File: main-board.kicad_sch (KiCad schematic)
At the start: 3 parts, among them J1 Battery, J25 Mikona

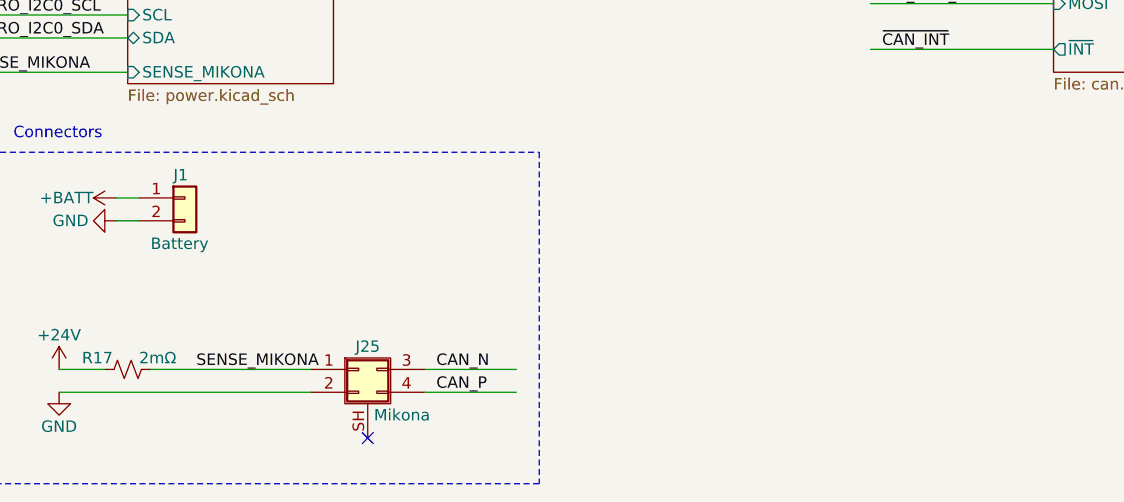
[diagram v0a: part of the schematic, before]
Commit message: Import the previous main board to match the overall shape, and re-annotate the schematic.
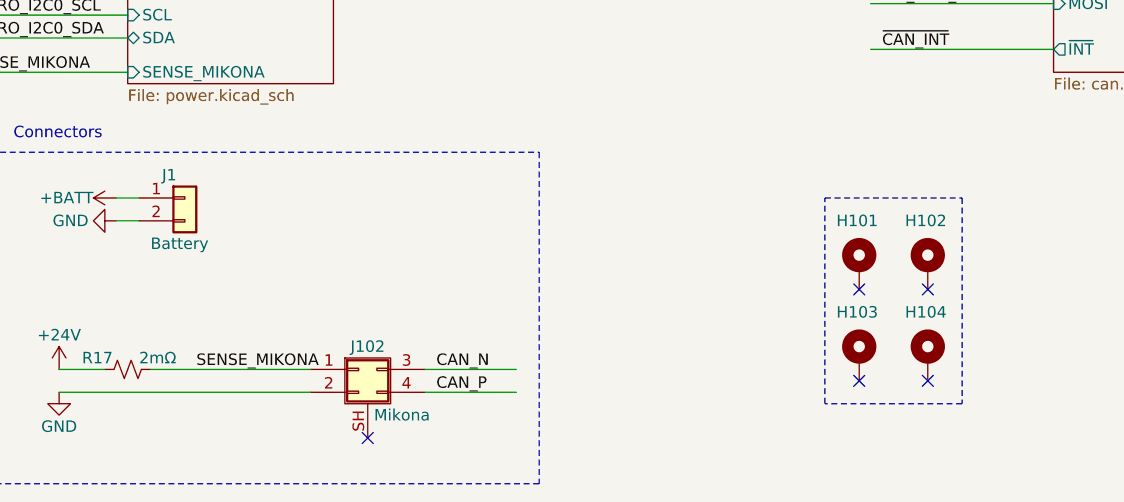
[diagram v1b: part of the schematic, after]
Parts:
- added H101, H102, H103, H104: MountingHole_Pad, MountingHole:MountingHole_3.2mm_M3_ISO14580_Pad, symbol Mechanical:MountingHole_Pad
- R17: footprint (none) -> Resistor_SMD:R_2512_6332Metric
- renumbered J25 to J102
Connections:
- no-connect marks 4 -> 8
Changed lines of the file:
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@@
 (kicad_sch (version 20230121) (generator eeschema)
   (paper "A4")
+  (no_connect (at 119.38 168.91))
   (no_connect (at 64.77 185.42))
+  (no_connect (at 119.38 179.07))
+  (no_connect (at 127 179.07))
   (no_connect (at 38.1 133.35))
   (no_connect (at 29.21 41.91))
   (no_connect (at 29.21 52.07))
+  (no_connect (at 127 168.91))
   (wire (pts (xy 120.65 134.62) (xy 140.97 134.62))
     (stroke (width 0) (type default))
@@
     (fill (type none))
   )
+  (rectangle (start 115.57 158.75) (end 130.81 181.61)
+    (stroke (width 0) (type dash))
+    (fill (type none))
+  )
   (text "Connectors" (at 25.4 152.4 0)
     (effects (font (size 1.27 1.27)) (justify left bottom))
@@
   (label "CM_SPI1_SCK" (at 121.92 132.08 0) (fields_autoplaced)
     (effects (font (size 1.27 1.27)) (justify left bottom))
+  )
+  (symbol (lib_id "Mechanical:MountingHole_Pad") (at 127 166.37 0) (unit 1)
+    (in_bom yes) (on_board yes) (dnp no)
+    (property "Reference" "H102" (at 124.46 161.29 0)
+      (effects (font (size 1.27 1.27)) (justify left))
+    )
+    (property "Value" "MountingHole_Pad" (at 129.54 167.005 0)
+      (effects (font (size 1.27 1.27)) (justify left) hide)
+    )
+    (property "Footprint" "MountingHole:MountingHole_3.2mm_M3_ISO14580_Pad" (at 127 166.37 0)
+      (effects (font (size 1.27 1.27)) hide)
+    )
+    (property "Datasheet" "~" (at 127 166.37 0)
+      (effects (font (size 1.27 1.27)) hide)
+    )
+    (pin "1")
+    (instances
+      (project "main-board"
+        (path "/5ad67b7d-c56f-4b00-8953-cc84f90f9708"
+          (reference "H102") (unit 1)
+        )
+      )
+    )
   )
   (symbol (lib_name "GND_1") (lib_id "power:GND") (at 36.83 161.29 270) (unit 1)
@@
         )
         (path "/5ad67b7d-c56f-4b00-8953-cc84f90f9708"
-          (reference "#PWR027") (unit 1)
+          (reference "#PWR0102") (unit 1)
         )
       )
@@
         )
         (path "/5ad67b7d-c56f-4b00-8953-cc84f90f9708"
-          (reference "#PWR023") (unit 1)
+          (reference "#PWR0101") (unit 1)
+        )
+      )
+    )
+  )
+  (symbol (lib_id "Mechanical:MountingHole_Pad") (at 119.38 176.53 0) (unit 1)
+    (in_bom yes) (on_board yes) (dnp no)
+    (property "Reference" "H103" (at 116.84 171.45 0)
+      (effects (font (size 1.27 1.27)) (justify left))
+    )
+    (property "Value" "MountingHole_Pad" (at 121.92 177.165 0)
+      (effects (font (size 1.27 1.27)) (justify left) hide)
+    )
+    (property "Footprint" "MountingHole:MountingHole_3.2mm_M3_ISO14580_Pad" (at 119.38 176.53 0)
+      (effects (font (size 1.27 1.27)) hide)
+    )
+    (property "Datasheet" "~" (at 119.38 176.53 0)
+      (effects (font (size 1.27 1.27)) hide)
+    )
+    (pin "1")
+    (instances
+      (project "main-board"
+        (path "/5ad67b7d-c56f-4b00-8953-cc84f90f9708"
+          (reference "H103") (unit 1)
         )
       )
@@
       (project "main-board"
         (path "/5ad67b7d-c56f-4b00-8953-cc84f90f9708"
-          (reference "#PWR0152") (unit 1)
+          (reference "#PWR0103") (unit 1)
         )
       )
@@
       (project "main-board"
         (path "/5ad67b7d-c56f-4b00-8953-cc84f90f9708"
-          (reference "#PWR0153") (unit 1)
+          (reference "#PWR0104") (unit 1)
+        )
+      )
+    )
+  )
+  (symbol (lib_id "Mechanical:MountingHole_Pad") (at 127 176.53 0) (unit 1)
+    (in_bom yes) (on_board yes) (dnp no)
+    (property "Reference" "H104" (at 124.46 171.45 0)
+      (effects (font (size 1.27 1.27)) (justify left))
+    )
+    (property "Value" "MountingHole_Pad" (at 129.54 177.165 0)
+      (effects (font (size 1.27 1.27)) (justify left) hide)
+    )
+    (property "Footprint" "MountingHole:MountingHole_3.2mm_M3_ISO14580_Pad" (at 127 176.53 0)
+      (effects (font (size 1.27 1.27)) hide)
+    )
+    (property "Datasheet" "~" (at 127 176.53 0)
+      (effects (font (size 1.27 1.27)) hide)
+    )
+    (pin "1")
+    (instances
+      (project "main-board"
+        (path "/5ad67b7d-c56f-4b00-8953-cc84f90f9708"
+          (reference "H104") (unit 1)
         )
       )
@@
   (symbol (lib_id "Connector_Generic_Shielded:Conn_02x02_Top_Bottom_Shielded") (at 63.5 177.8 0) (unit 1)
     (in_bom yes) (on_board yes) (dnp no)
-    (property "Reference" "J25" (at 64.77 175.26 0)
+    (property "Reference" "J102" (at 64.77 175.26 0)
       (effects (font (size 1.27 1.27)))
     )
@@
       (project "main-board"
         (path "/5ad67b7d-c56f-4b00-8953-cc84f90f9708"
-          (reference "J25") (unit 1)
+          (reference "J102") (unit 1)
         )
       )
@@
       (effects (font (size 1.27 1.27)) (justify left))
     )
-    (property "Footprint" "" (at 38.1 177.8 0)
+    (property "Footprint" "Resistor_SMD:R_2512_6332Metric" (at 38.1 177.8 0)
       (effects (font (size 1.27 1.27)) hide)
     )
@@
         )
         (path "/5ad67b7d-c56f-4b00-8953-cc84f90f9708"
-          (reference "R31") (unit 1)
+          (reference "R101") (unit 1)
         )
       )
@@
   (symbol (lib_id "Connector_Generic:Conn_01x02") (at 44.45 158.75 0) (unit 1)
     (in_bom yes) (on_board yes) (dnp no)
-    (property "Reference" "J1" (at 43.18 156.21 0)
+    (property "Reference" "J1" (at 41.91 156.21 0)
       (effects (font (size 1.27 1.27)) (justify left))
     )
@@
         )
         (path "/5ad67b7d-c56f-4b00-8953-cc84f90f9708"
-          (reference "J1") (unit 1)
+          (reference "J101") (unit 1)
+        )
+      )
+    )
+  )
+  (symbol (lib_id "Mechanical:MountingHole_Pad") (at 119.38 166.37 0) (unit 1)
+    (in_bom yes) (on_board yes) (dnp no)
+    (property "Reference" "H101" (at 116.84 161.29 0)
+      (effects (font (size 1.27 1.27)) (justify left))
+    )
+    (property "Value" "MountingHole_Pad" (at 121.92 167.005 0)
+      (effects (font (size 1.27 1.27)) (justify left) hide)
+    )
+    (property "Footprint" "MountingHole:MountingHole_3.2mm_M3_ISO14580_Pad" (at 119.38 166.37 0)
+      (effects (font (size 1.27 1.27)) hide)
+    )
+    (property "Datasheet" "~" (at 119.38 166.37 0)
+      (effects (font (size 1.27 1.27)) hide)
+    )
+    (pin "1")
+    (instances
+      (project "main-board"
+        (path "/5ad67b7d-c56f-4b00-8953-cc84f90f9708"
+          (reference "H101") (unit 1)
         )
       )
@@
     (instances
       (project "main-board"
-        (path "/5ad67b7d-c56f-4b00-8953-cc84f90f9708" (page "7"))
+        (path "/5ad67b7d-c56f-4b00-8953-cc84f90f9708" (page "5"))
       )
     )
@@
     (instances
       (project "main-board"
-        (path "/5ad67b7d-c56f-4b00-8953-cc84f90f9708" (page "5"))
+        (path "/5ad67b7d-c56f-4b00-8953-cc84f90f9708" (page "4"))
       )
     )
@@
     (instances
       (project "main-board"
-        (path "/5ad67b7d-c56f-4b00-8953-cc84f90f9708" (page "11"))
+        (path "/5ad67b7d-c56f-4b00-8953-cc84f90f9708" (page "7"))
       )
     )
@@
     (instances
       (project "main-board"
-        (path "/5ad67b7d-c56f-4b00-8953-cc84f90f9708" (page "8"))
-      )
-    )
+        (path "/5ad67b7d-c56f-4b00-8953-cc84f90f9708" (page "6"))
+      )
+    )

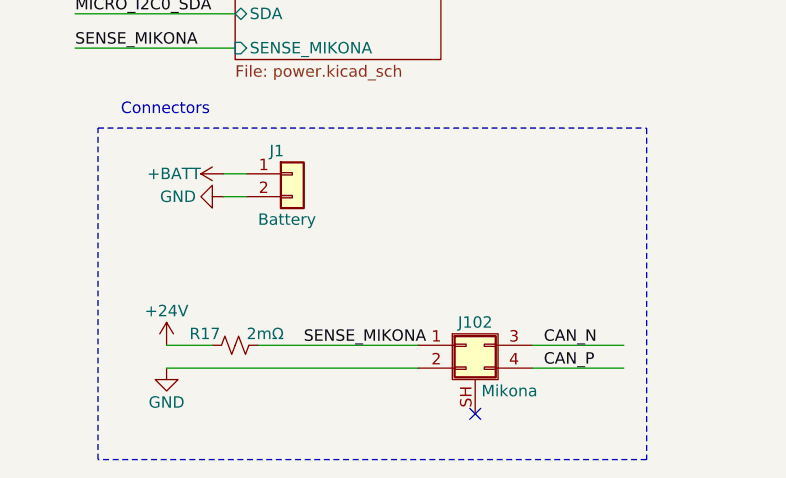
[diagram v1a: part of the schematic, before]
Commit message: Place all the components on the PCB.
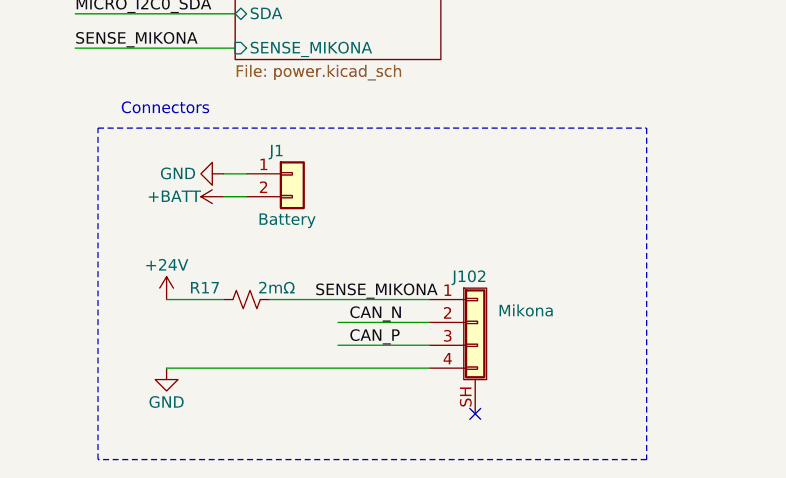
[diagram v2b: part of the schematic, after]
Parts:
- removed J102: Mikona, 1054291104:MOLEX_1054291104, symbol Connector_Generic_Shielded:Conn_02x02_Top_Bottom_Shielded
- added J102: Mikona, 1054301204:MOLEX_1054301204, symbol Connector_Generic_Shielded:Conn_01x04_Shielded
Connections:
- net +BATT: now also J1.2 (Pin_2); no longer J1.1 (Pin_1)
- net CAN_N: now also J102.2 (Pin_2)
- net CAN_P: now also J102.3 (Pin_3)
- net GND: now also J1.1 (Pin_1), J102.4 (Pin_4); no longer J1.2 (Pin_2)
- net SENSE_MIKONA: now also J102.1 (Pin_1)
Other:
- moved on the sheet: R17

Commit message: Finish the draft routing.
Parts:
- removed R17: 2mΩ, Resistor_SMD:R_2512_6332Metric, symbol Device:R_Small_US
- J102: symbol Connector_Generic_Shielded:Conn_01x04_Shielded -> Connector_Generic:Conn_01x04
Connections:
- net CAN_N is gone; now on net MICRO_I2C0_SCL: J102.2 (Pin_2)
- net CAN_P is gone; now on net MICRO_I2C0_SDA: J102.3 (Pin_3)
- net SENSE_MIKONA is gone; now on net +24V: J102.1 (Pin_1)
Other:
- removed sheet CAN
- sheet Power ports: added none; removed PWR_STATUS, SENSE_MIKONA

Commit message: Fix the issues found during testing in schematics.
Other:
- sheet Compute Module ports: added GPIO26; removed GPIO3
- sheet Micro ports: added CM_INT, LED_SWITCH; removed IR
- sheet Power ports: added LED_SWITCH; removed none
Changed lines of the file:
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@@
   (paper "A4")
   (no_connect (at 119.38 168.91))
-  (no_connect (at 29.21 54.61))
+  (no_connect (at 29.21 67.31))
   (no_connect (at 67.31 35.56))
   (no_connect (at 119.38 179.07))
@@
     (stroke (width 0) (type default))
   )
+  (wire (pts (xy 107.95 48.26) (xy 128.27 48.26))
+    (stroke (width 0) (type default))
+  )
   (wire (pts (xy 67.31 41.91) (xy 82.55 41.91))
     (stroke (width 0) (type default))
@@
     (stroke (width 0) (type default))
   )
+  (wire (pts (xy 60.96 134.62) (xy 78.74 134.62))
+    (stroke (width 0) (type default))
+  )
   (wire (pts (xy 214.63 35.56) (xy 222.25 35.56))
     (stroke (width 0) (type default))
@@
     (stroke (width 0) (type default))
   )
+  (wire (pts (xy 172.72 76.2) (xy 190.5 76.2))
+    (stroke (width 0) (type default))
+  )
   (wire (pts (xy 118.11 102.87) (xy 135.89 102.87))
     (stroke (width 0) (type default))
@@
     (stroke (width 0) (type default))
   )
-  (wire (pts (xy 17.78 64.77) (xy 29.21 64.77))
-    (stroke (width 0) (type default))
-  )
   (wire (pts (xy 113.03 41.91) (xy 128.27 41.91))
     (stroke (width 0) (type default))
@@
     (stroke (width 0) (type default))
   )
-  (wire (pts (xy 118.11 77.47) (xy 128.27 77.47))
-    (stroke (width 0) (type default))
-  )
   (wire (pts (xy 67.31 77.47) (xy 82.55 77.47))
+    (stroke (width 0) (type default))
+  )
+  (wire (pts (xy 15.24 64.77) (xy 29.21 64.77))
     (stroke (width 0) (type default))
   )
@@
     (effects (font (size 1.27 1.27)) (justify left bottom))
   )
+  (label "CM_MICRO_INT" (at 15.24 64.77 0) (fields_autoplaced)
+    (effects (font (size 1.27 1.27)) (justify left bottom))
+  )
   (label "M_SPI_MISO" (at 68.58 80.01 0) (fields_autoplaced)
     (effects (font (size 1.27 1.27)) (justify left bottom))
@@
     (effects (font (size 1.27 1.27)) (justify left bottom))
   )
+  (label "LED_POWER_LOW" (at 62.23 134.62 0) (fields_autoplaced)
+    (effects (font (size 1.27 1.27)) (justify left bottom))
+  )
   (label "CM_SPI1_MOSI" (at 107.95 58.42 0) (fields_autoplaced)
     (effects (font (size 1.27 1.27)) (justify left bottom))
   )
+  (label "LED_POWER_LOW" (at 173.99 76.2 0) (fields_autoplaced)
+    (effects (font (size 1.27 1.27)) (justify left bottom))
+  )
   (label "M_EN" (at 215.9 81.28 0) (fields_autoplaced)
     (effects (font (size 1.27 1.27)) (justify left bottom))
@@
     (effects (font (size 1.27 1.27)) (justify left bottom))
   )
-  (label "IR" (at 17.78 64.77 0) (fields_autoplaced)
-    (effects (font (size 1.27 1.27)) (justify left bottom))
-  )
   (label "MICRO_I2C1_SCL" (at 172.72 110.49 0) (fields_autoplaced)
     (effects (font (size 1.27 1.27)) (justify left bottom))
@@
     (effects (font (size 1.27 1.27)) (justify left bottom))
   )
-  (label "IR" (at 118.11 77.47 0) (fields_autoplaced)
-    (effects (font (size 1.27 1.27)) (justify left bottom))
-  )
   (label "IR_ADC" (at 118.11 80.01 0) (fields_autoplaced)
     (effects (font (size 1.27 1.27)) (justify left bottom))
@@
   )
   (label "M_SPI_MISO" (at 273.05 48.26 0) (fields_autoplaced)
+    (effects (font (size 1.27 1.27)) (justify left bottom))
+  )
+  (label "CM_MICRO_INT" (at 107.95 48.26 0) (fields_autoplaced)
     (effects (font (size 1.27 1.27)) (justify left bottom))
   )
@@
       (effects (font (size 1.27 1.27)) (justify left))
     )
-    (pin "IR" output (at 128.27 77.47 180)
-      (effects (font (size 1.27 1.27)) (justify left))
-    )
     (pin "M3_CTRL_STATUS" input (at 172.72 54.61 0)
       (effects (font (size 1.27 1.27)) (justify right))
@@
     (pin "I2C1_SCL" output (at 128.27 69.85 180)
       (effects (font (size 1.27 1.27)) (justify left))
+    )
+    (pin "CM_INT" output (at 128.27 48.26 180)
+      (effects (font (size 1.27 1.27)) (justify left))
+    )
+    (pin "LED_SWITCH" output (at 172.72 76.2 0)
+      (effects (font (size 1.27 1.27)) (justify right))
     )
     (instances
@@
       (effects (font (size 1.27 1.27)) (justify left))
     )
+    (pin "LED_SWITCH" input (at 60.96 134.62 0)
+      (effects (font (size 1.27 1.27)) (justify right))
+    )
     (instances
       (project "main-board"
@@
       (effects (font (size 1.27 1.27)) (justify right))
     )
-    (pin "GPIO3" bidirectional (at 29.21 54.61 180)
-      (effects (font (size 1.27 1.27)) (justify left))
-    )
     (pin "GPIO2" bidirectional (at 29.21 52.07 180)
       (effects (font (size 1.27 1.27)) (justify left))
     )
+    (pin "GPIO26" bidirectional (at 29.21 67.31 180)
+      (effects (font (size 1.27 1.27)) (justify left))
+    )
